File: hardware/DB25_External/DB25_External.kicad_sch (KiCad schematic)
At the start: 57 parts, among them J2 DB25_Male_MountingHoles, U3 AMS1117-2.85, U4 LVT245, U5 LVT125, U6 LVT125, U7 LVT125, U9 LVT245

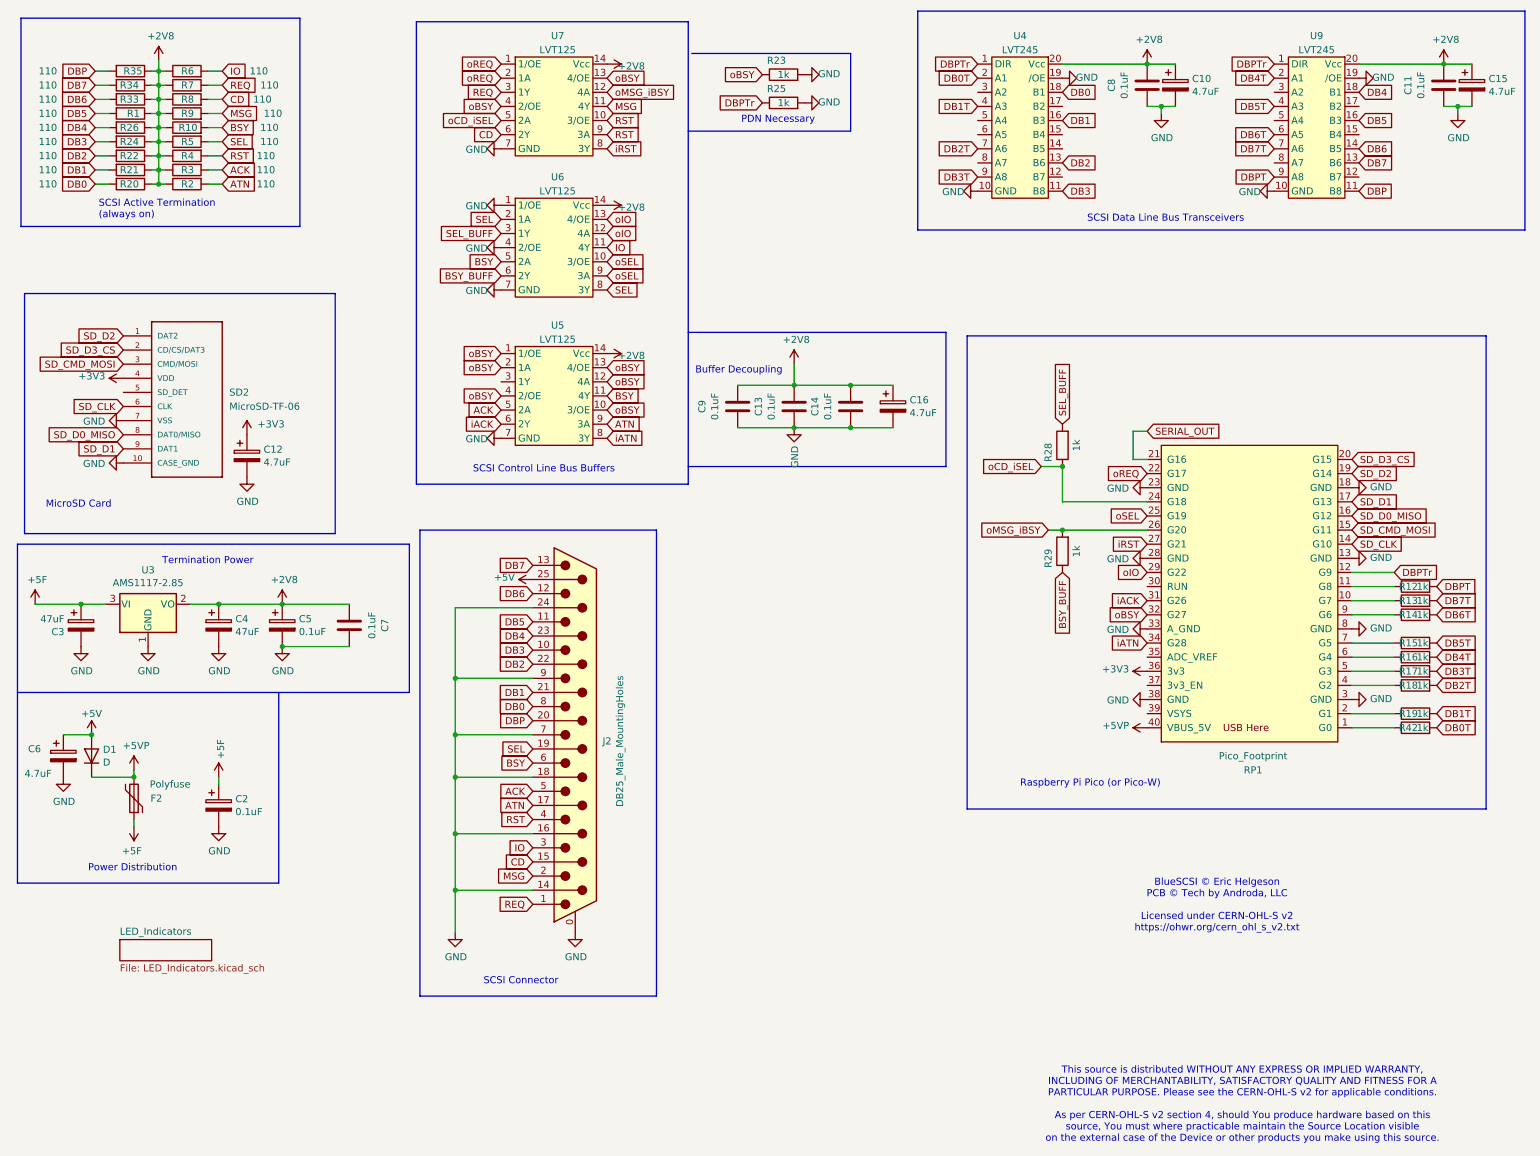
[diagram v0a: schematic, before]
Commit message: My version sent to Aisler, pico under the PCB
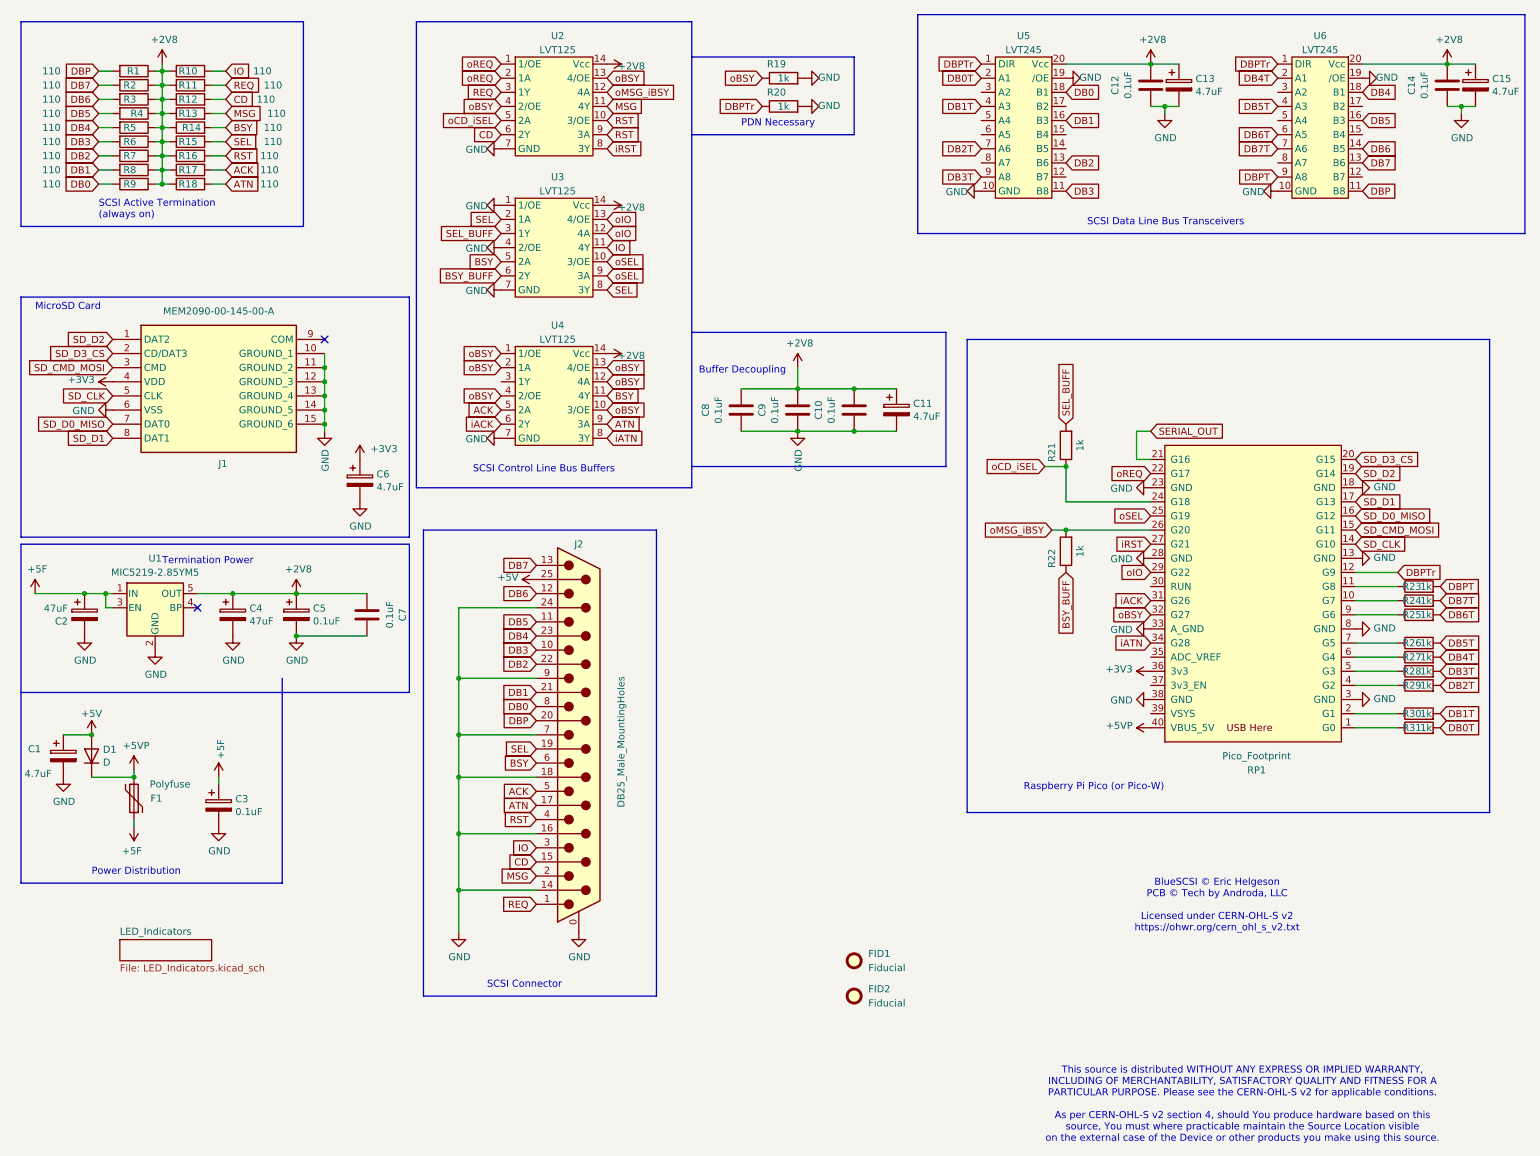
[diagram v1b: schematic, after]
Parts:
- removed SD2: MicroSD-TF-06, Library:TF-06_MicroSD, symbol New_Library:MicroSD-TF-06
- removed U3: AMS1117-2.85, Package_TO_SOT_SMD:SOT-223-3_TabPin2, symbol Regulator_Linear:AMS1117CD-2.85
- added FID1, FID2: Fiducial, Fiducial:Fiducial_0.5mm_Mask1.5mm, symbol Mechanical:Fiducial
- added J1: MEM2090-00-145-00-A, Library:MEM20900014500A, symbol MEM2090-00-145-00-A:MEM2090-00-145-00-A
- added U1: MIC5219-2.85YM5, Package_TO_SOT_SMD:SOT-23-5, symbol Regulator_Linear:MIC5219-2.85YM5
- C1: renamed from C6; footprint Capacitor_SMD:C_0805_2012Metric_Pad1.15x1.40mm_HandSolder -> Capacitor_SMD:C_0805_2012Metric_Pad1.18x1.45mm_HandSolder
- C10: renamed from C14; footprint Capacitor_SMD:C_0603_1608Metric_Pad1.08x0.95mm_HandSolder -> Capacitor_SMD:C_0805_2012Metric_Pad1.18x1.45mm_HandSolder
- C2: renamed from C3; footprint Capacitor_SMD:C_1206_3216Metric_Pad1.42x1.75mm_HandSolder -> Capacitor_SMD:C_1206_3216Metric_Pad1.33x1.80mm_HandSolder
- C3: renamed from C2; footprint Capacitor_SMD:C_0805_2012Metric_Pad1.15x1.40mm_HandSolder -> Capacitor_SMD:C_0805_2012Metric_Pad1.18x1.45mm_HandSolder
- C4: footprint Capacitor_SMD:C_1206_3216Metric_Pad1.42x1.75mm_HandSolder -> Capacitor_SMD:C_1206_3216Metric_Pad1.33x1.80mm_HandSolder
- C5: footprint Capacitor_SMD:C_0805_2012Metric_Pad1.15x1.40mm_HandSolder -> Capacitor_SMD:C_0805_2012Metric_Pad1.18x1.45mm_HandSolder
- C6: renamed from C12; footprint Capacitor_SMD:C_0805_2012Metric_Pad1.15x1.40mm_HandSolder -> Capacitor_SMD:C_0805_2012Metric_Pad1.18x1.45mm_HandSolder
- C7: footprint Capacitor_SMD:C_0603_1608Metric_Pad1.08x0.95mm_HandSolder -> Capacitor_SMD:C_0805_2012Metric_Pad1.18x1.45mm_HandSolder
- C8: renamed from C9; footprint Capacitor_SMD:C_0603_1608Metric_Pad1.08x0.95mm_HandSolder -> Capacitor_SMD:C_0805_2012Metric_Pad1.18x1.45mm_HandSolder
- C9: renamed from C13; footprint Capacitor_SMD:C_0603_1608Metric_Pad1.08x0.95mm_HandSolder -> Capacitor_SMD:C_0805_2012Metric_Pad1.18x1.45mm_HandSolder
- D1: footprint Diode_SMD:D_SMA -> Diode_SMD:D_SMA_Handsoldering
- J2: footprint Connector_Dsub:DSUB-25_Male_Horizontal_P2.77x2.84mm_EdgePinOffset7.70mm_Housed_MountingHolesOffset9.12mm -> Library:DSUB-25_Male_Horizontal_middle_mount
- R1: renamed from R35; footprint Resistor_SMD:R_0603_1608Metric_Pad0.98x0.95mm_HandSolder -> Resistor_SMD:R_0805_2012Metric_Pad1.20x1.40mm_HandSolder
- R10: renamed from R6; footprint Resistor_SMD:R_0603_1608Metric_Pad0.98x0.95mm_HandSolder -> Resistor_SMD:R_0805_2012Metric_Pad1.20x1.40mm_HandSolder
- R11: renamed from R7; footprint Resistor_SMD:R_0603_1608Metric_Pad0.98x0.95mm_HandSolder -> Resistor_SMD:R_0805_2012Metric_Pad1.20x1.40mm_HandSolder
- R12: renamed from R8; footprint Resistor_SMD:R_0603_1608Metric_Pad0.98x0.95mm_HandSolder -> Resistor_SMD:R_0805_2012Metric_Pad1.20x1.40mm_HandSolder
- R13: renamed from R9; footprint Resistor_SMD:R_0603_1608Metric_Pad0.98x0.95mm_HandSolder -> Resistor_SMD:R_0805_2012Metric_Pad1.20x1.40mm_HandSolder
- R14: renamed from R10; footprint Resistor_SMD:R_0603_1608Metric_Pad0.98x0.95mm_HandSolder -> Resistor_SMD:R_0805_2012Metric_Pad1.20x1.40mm_HandSolder
- R15: renamed from R5; footprint Resistor_SMD:R_0603_1608Metric_Pad0.98x0.95mm_HandSolder -> Resistor_SMD:R_0805_2012Metric_Pad1.20x1.40mm_HandSolder
- R16: renamed from R4; footprint Resistor_SMD:R_0603_1608Metric_Pad0.98x0.95mm_HandSolder -> Resistor_SMD:R_0805_2012Metric_Pad1.20x1.40mm_HandSolder
- R17: renamed from R3; footprint Resistor_SMD:R_0603_1608Metric_Pad0.98x0.95mm_HandSolder -> Resistor_SMD:R_0805_2012Metric_Pad1.20x1.40mm_HandSolder
- R18: renamed from R2; footprint Resistor_SMD:R_0603_1608Metric_Pad0.98x0.95mm_HandSolder -> Resistor_SMD:R_0805_2012Metric_Pad1.20x1.40mm_HandSolder
- R19: renamed from R23; footprint Resistor_SMD:R_0603_1608Metric_Pad0.98x0.95mm_HandSolder -> Resistor_SMD:R_0805_2012Metric_Pad1.20x1.40mm_HandSolder
- R2: renamed from R34; footprint Resistor_SMD:R_0603_1608Metric_Pad0.98x0.95mm_HandSolder -> Resistor_SMD:R_0805_2012Metric_Pad1.20x1.40mm_HandSolder
- R20: renamed from R25; footprint Resistor_SMD:R_0603_1608Metric_Pad0.98x0.95mm_HandSolder -> Resistor_SMD:R_0805_2012Metric_Pad1.20x1.40mm_HandSolder
- R21: renamed from R28; footprint Resistor_SMD:R_0603_1608Metric_Pad0.98x0.95mm_HandSolder -> Resistor_SMD:R_0805_2012Metric_Pad1.20x1.40mm_HandSolder
- R22: renamed from R29; footprint Resistor_SMD:R_0603_1608Metric_Pad0.98x0.95mm_HandSolder -> Resistor_SMD:R_0805_2012Metric_Pad1.20x1.40mm_HandSolder
- R23: renamed from R12; footprint Resistor_SMD:R_0603_1608Metric_Pad0.98x0.95mm_HandSolder -> Resistor_SMD:R_0805_2012Metric_Pad1.20x1.40mm_HandSolder
- R24: renamed from R13; footprint Resistor_SMD:R_0603_1608Metric_Pad0.98x0.95mm_HandSolder -> Resistor_SMD:R_0805_2012Metric_Pad1.20x1.40mm_HandSolder
- R25: renamed from R14; footprint Resistor_SMD:R_0603_1608Metric_Pad0.98x0.95mm_HandSolder -> Resistor_SMD:R_0805_2012Metric_Pad1.20x1.40mm_HandSolder
- R26: renamed from R15; footprint Resistor_SMD:R_0603_1608Metric_Pad0.98x0.95mm_HandSolder -> Resistor_SMD:R_0805_2012Metric_Pad1.20x1.40mm_HandSolder
- R27: renamed from R16; footprint Resistor_SMD:R_0603_1608Metric_Pad0.98x0.95mm_HandSolder -> Resistor_SMD:R_0805_2012Metric_Pad1.20x1.40mm_HandSolder
- R28: renamed from R17; footprint Resistor_SMD:R_0603_1608Metric_Pad0.98x0.95mm_HandSolder -> Resistor_SMD:R_0805_2012Metric_Pad1.20x1.40mm_HandSolder
- R29: renamed from R18; footprint Resistor_SMD:R_0603_1608Metric_Pad0.98x0.95mm_HandSolder -> Resistor_SMD:R_0805_2012Metric_Pad1.20x1.40mm_HandSolder
- R3: renamed from R33; footprint Resistor_SMD:R_0603_1608Metric_Pad0.98x0.95mm_HandSolder -> Resistor_SMD:R_0805_2012Metric_Pad1.20x1.40mm_HandSolder
- R30: renamed from R19; footprint Resistor_SMD:R_0603_1608Metric_Pad0.98x0.95mm_HandSolder -> Resistor_SMD:R_0805_2012Metric_Pad1.20x1.40mm_HandSolder
- R31: renamed from R42; footprint Resistor_SMD:R_0603_1608Metric_Pad0.98x0.95mm_HandSolder -> Resistor_SMD:R_0805_2012Metric_Pad1.20x1.40mm_HandSolder
- R4: renamed from R1; footprint Resistor_SMD:R_0603_1608Metric_Pad0.98x0.95mm_HandSolder -> Resistor_SMD:R_0805_2012Metric_Pad1.20x1.40mm_HandSolder
- R5: renamed from R26; footprint Resistor_SMD:R_0603_1608Metric_Pad0.98x0.95mm_HandSolder -> Resistor_SMD:R_0805_2012Metric_Pad1.20x1.40mm_HandSolder
- R6: renamed from R24; footprint Resistor_SMD:R_0603_1608Metric_Pad0.98x0.95mm_HandSolder -> Resistor_SMD:R_0805_2012Metric_Pad1.20x1.40mm_HandSolder
- R7: renamed from R22; footprint Resistor_SMD:R_0603_1608Metric_Pad0.98x0.95mm_HandSolder -> Resistor_SMD:R_0805_2012Metric_Pad1.20x1.40mm_HandSolder
- R8: renamed from R21; footprint Resistor_SMD:R_0603_1608Metric_Pad0.98x0.95mm_HandSolder -> Resistor_SMD:R_0805_2012Metric_Pad1.20x1.40mm_HandSolder
- R9: renamed from R20; footprint Resistor_SMD:R_0603_1608Metric_Pad0.98x0.95mm_HandSolder -> Resistor_SMD:R_0805_2012Metric_Pad1.20x1.40mm_HandSolder
- renumbered C16 to C11, C8 to C12, C10 to C13, C11 to C14, F2 to F1, U7 to U2, U6 to U3, U5 to U4, U4 to U5, U9 to U6
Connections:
- net +2V8: now also U1.5 (OUT)
- net +3V3: now also J1.4 (VDD)
- net +5F: now also U1.1 (IN), U1.3 (EN)
- net GND: now also J1.10 (GROUND_1), J1.11 (GROUND_2), J1.12 (GROUND_3), J1.13 (GROUND_4), J1.14 (GROUND_5), J1.15 (GROUND_6), J1.6 (VSS), U1.2 (GND)
- net SD_CLK: now also J1.5 (CLK)
- net SD_CMD_MOSI: now also J1.3 (CMD)
- net SD_D0_MISO: now also J1.7 (DAT0)
- net SD_D1: now also J1.8 (DAT1)
- net SD_D2: now also J1.1 (DAT2)
- net SD_D3_CS: now also J1.2 (CD/DAT3)
- no-connect marks 0 -> 2
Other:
- moved on the sheet: C10, C11, C12, C13, C14, C15, C2, C4, C5, C6, C7, C8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

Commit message: Clean up
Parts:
- J2: value DB25_Male_MountingHoles -> DB25_Male
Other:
- title: BlueSCSI V2, DB25 External 2024.01a -> Forked from BlueSCSI V2, DB25 External 2024.01a
- moved on the sheet: C1, C10, C11, C3, C6, C8, C9, D1, F1, J1
